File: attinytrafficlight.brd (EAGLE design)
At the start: 24.1 x 17.8 mm, 12 parts, among them U1 Tiny85-20-SMT

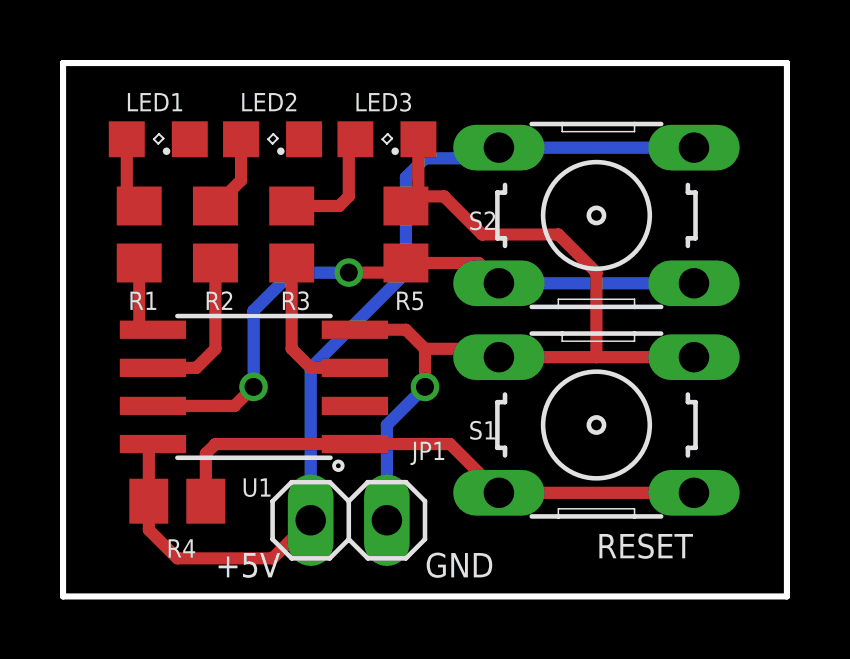
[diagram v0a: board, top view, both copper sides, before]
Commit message: add author and version on silk
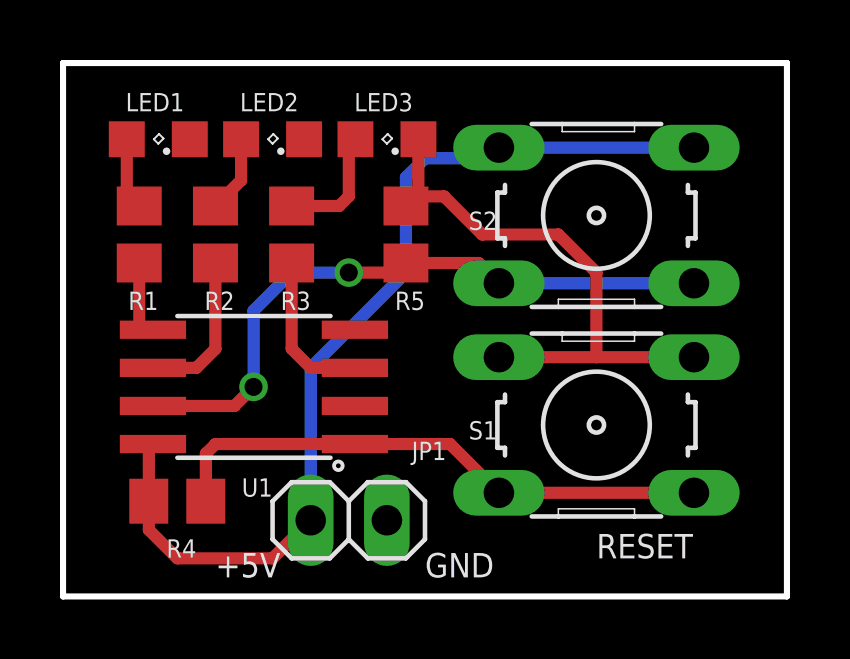
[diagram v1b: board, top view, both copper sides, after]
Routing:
- net GND: track 30.2 -> 18.8 mm, vias 1 -> 0
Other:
- board text added: "Emil Bergold"
- board text added: "V1.0"
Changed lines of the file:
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@@
 <text x="31.115" y="54.61" size="0.8128" layer="21" font="vector" ratio="15">GND</text>
 <text x="20.955" y="71.12" size="1.016" layer="22" font="vector" ratio="15" rot="SMR270">ATtiny Traffic Light</text>
+<text x="22.225" y="71.12" size="0.8128" layer="22" font="vector" ratio="15" rot="SMR270">V1.0</text>
+<text x="22.225" y="54.61" size="0.8128" layer="22" font="vector" ratio="15" rot="SMR270" align="bottom-right">Emil Bergold</text>
 </plain>
 <attributes>
@@
 <wire x1="30.895" y1="69.215" x2="30.895" y2="67.405" width="0.4064" layer="1"/>
 <wire x1="30.895" y1="67.405" x2="30.8" y2="67.31" width="0.4064" layer="1"/>
-<wire x1="28.7782" y1="62.865" x2="30.48" y2="62.865" width="0.4064" layer="1"/>
-<wire x1="31.115" y1="62.23" x2="33.2994" y2="62.23" width="0.4064" layer="1"/>
-<wire x1="33.2994" y1="62.23" x2="33.5788" y2="61.9506" width="0.4064" layer="1"/>
 <wire x1="30.8" y1="67.31" x2="30.48" y2="66.99" width="0.4064" layer="1"/>
 <wire x1="30.8" y1="67.31" x2="31.75" y2="67.31" width="0.4064" layer="1"/>
 <wire x1="31.75" y1="67.31" x2="33.02" y2="66.04" width="0.4064" layer="1"/>
-<wire x1="29.845" y1="56.515" x2="29.845" y2="59.69" width="0.4064" layer="16"/>
-<wire x1="29.845" y1="59.69" x2="31.115" y2="60.96" width="0.4064" layer="16"/>
-<via x="31.115" y="60.96" extent="1-16" drill="0.6"/>
-<wire x1="31.115" y1="60.96" x2="31.115" y2="62.23" width="0.4064" layer="1"/>
-<wire x1="31.115" y1="62.23" x2="30.48" y2="62.865" width="0.4064" layer="1"/>
 <wire x1="33.5788" y1="61.9506" x2="36.83" y2="61.9506" width="0.4064" layer="1"/>
 <wire x1="36.83" y1="61.9506" x2="40.0812" y2="61.9506" width="0.4064" layer="1"/>
